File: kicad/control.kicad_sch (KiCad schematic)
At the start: 6 parts, among them U1 ATF22V10C-7PX, U17 SN74F377AN, U2 ATF22V10C-7PX

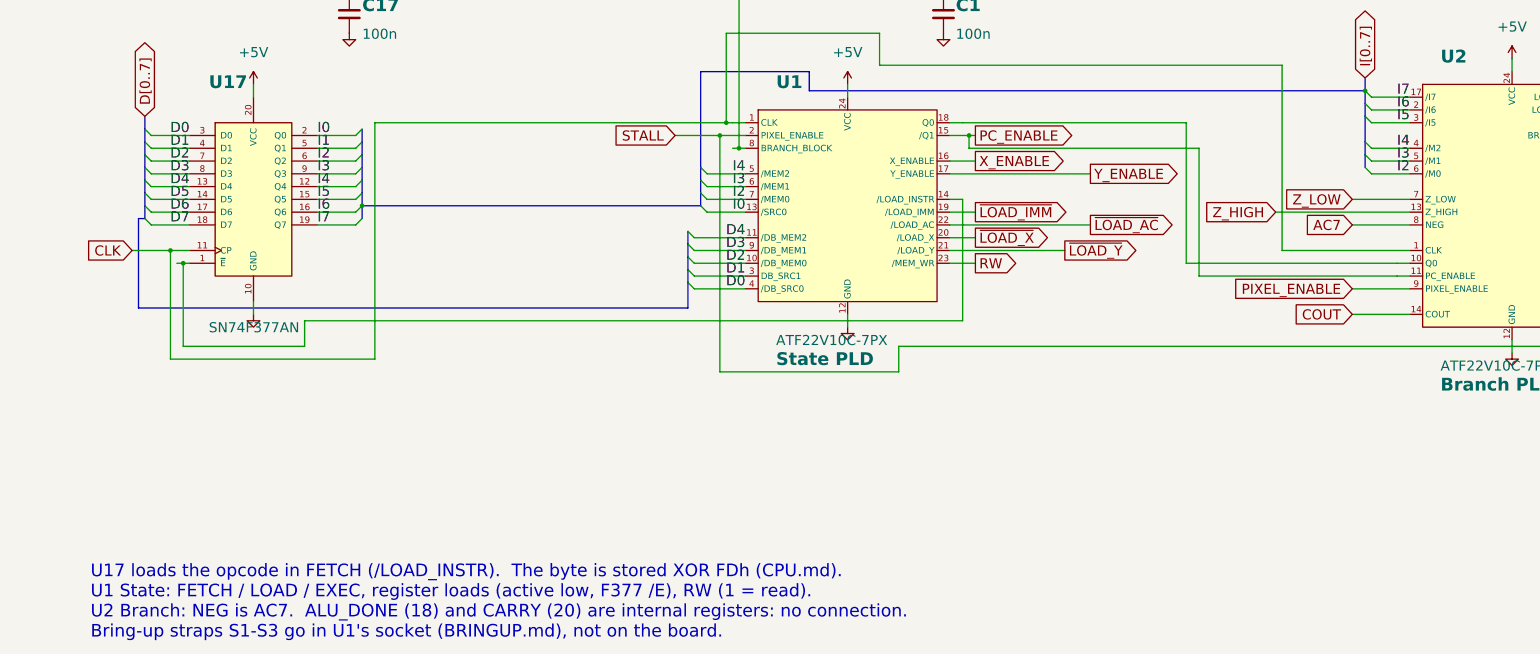
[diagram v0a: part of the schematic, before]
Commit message: Revert the opcode XOR: plain encoding, the cartridge 74AC541 is back
Justin found the inverted opcode bytes too confusing, and a pulled-low
bus is not practical, so this undoes 63a428c:
- opcode bytes are the plain fields again (nop = 02h); the cartridge's
  74AC541 drives 02h while it loads (6 chips, about 33 ms)
- State and Branch PLD revision 15, ALU revision 07 and cartridge PLD
  revision 03 have the same logic as 13, 13, 05 and 01
- read bus pull-ups 10k again; bring-up colour pull-downs 1k
- cartridge schematic gets U6 (74AC541), data bus SIP 10k
- program hex, menu ROM and bring-up ROM reassembled

Kept from 63a428c: RUN starts high in basys_top, the bring-up ROM's
explicit jump to frame_loop, and test_io's con_gets ROM map.

Co-Authored-By: Claude Opus 5.5 (1M context) <noreply@anthropic.com>
Claude-Session: https://claude.ai/code/session_01PNJoPfzmo1tu8EorCrua96
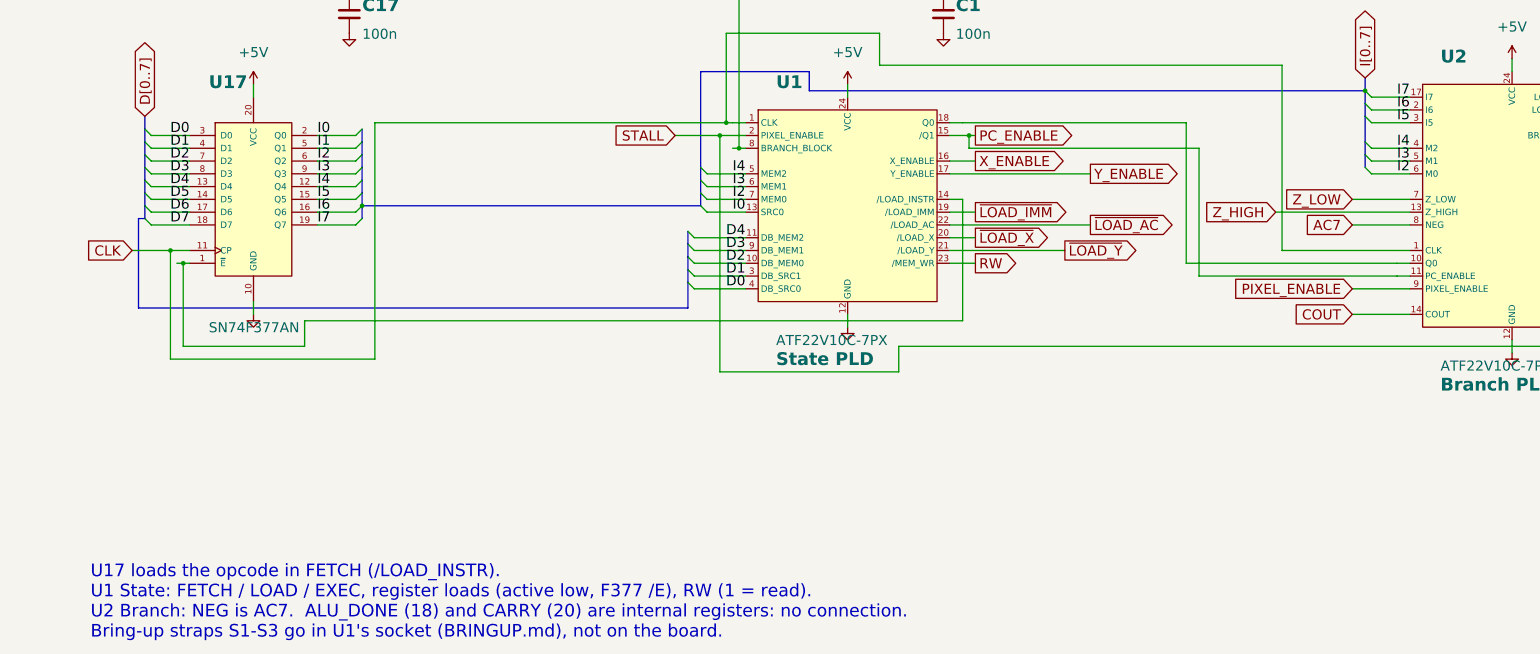
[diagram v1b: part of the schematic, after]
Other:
- note added: "U17 loads the opcode in FETCH (/LOAD_INSTR)."
- note removed: "U17 loads the opcode in FETCH (/LOAD_INSTR). The byte is stored XOR FDh (CPU.md)."
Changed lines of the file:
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@@
 (kicad_sch (version 20230121) (generator eeschema)
   (paper "A3")
-  (title_block (title "Placard: Control") (date "2026-10-20") (rev "1") (company "Placard computer") (comment 1 "Generated by src/scripts/gen_kicad_schematic.py; plan in docs/SCHEMATIC_PLAN.md") (comment 2 "Chip numbers U1-U41 = docs/CHIPS.md; decoupling Cn goes with Un"))
+  (title_block (title "Placard: Control") (date "2026-10-21") (rev "1") (company "Placard computer") (comment 1 "Generated by src/scripts/gen_kicad_schematic.py; plan in docs/SCHEMATIC_PLAN.md") (comment 2 "Chip numbers U1-U41 = docs/CHIPS.md; decoupling Cn goes with Un"))
   (text "Control" (at 15 22 0) (effects (font (size 6 6) bold) (justify left bottom)))
   (text "State and Branch PLDs, instruction register" (at 15 30 0) (effects (font (size 3 3)) (justify left bottom)))
@@
   (symbol (lib_id "power:GND") (at 341.63 96.52 0) (unit 1) (in_bom yes) (on_board yes) (dnp no) (property "Reference" "#PWR0312" (at 341.63 96.52 0) (effects (font (size 1.27 1.27)) hide)) (property "Value" "GND" (at 341.63 102.87 0) (effects (font (size 2 2)) hide)) (property "Footprint" "" (at 341.63 96.52 0) (effects (font (size 1.27 1.27)) hide)) (property "Datasheet" "" (at 341.63 96.52 0) (effects (font (size 1.27 1.27)) hide)) (pin "1") (instances (project "placard" (path "/e3450542-4ffc-59d4-a4a7-45636233928a/370d9988-af17-5e05-8c50-5ef0ca792654" (reference "#PWR0312") (unit 1)))))
   (symbol (lib_id "Device:C") (at 341.63 92.71 0) (unit 1) (in_bom yes) (on_board yes) (dnp no) (property "Reference" "C2" (at 344 92.42 0) (effects (font (size 2.54 2.54) bold) (justify left bottom))) (property "Value" "100n" (at 344 95.52 0) (effects (font (size 2 2)) (justify left top))) (property "Footprint" "Capacitor_THT:C_Disc_D5.0mm_W2.5mm_P5.00mm" (at 341.63 92.71 0) (effects (font (size 1.27 1.27)) hide)) (property "Datasheet" "~" (at 341.63 92.71 0) (effects (font (size 1.27 1.27)) hide)) (pin "1") (pin "2") (instances (project "placard" (path "/e3450542-4ffc-59d4-a4a7-45636233928a/370d9988-af17-5e05-8c50-5ef0ca792654" (reference "C2") (unit 1)))))
-  (text "U17 loads the opcode in FETCH (/LOAD_INSTR).  The byte is stored XOR FDh (CPU.md)." (at 40 205 0) (effects (font (size 2.5 2.5)) (justify left bottom)))
+  (text "U17 loads the opcode in FETCH (/LOAD_INSTR)." (at 40 205 0) (effects (font (size 2.5 2.5)) (justify left bottom)))
   (text "U1 State: FETCH / LOAD / EXEC, register loads (active low, F377 /E), RW (1 = read)." (at 40 209 0) (effects (font (size 2.5 2.5)) (justify left bottom)))
   (text "U2 Branch: NEG is AC7.  ALU_DONE (18) and CARRY (20) are internal registers: no connection." (at 40 213 0) (effects (font (size 2.5 2.5)) (justify left bottom)))

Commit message: Cartridge loader everywhere: FPGA cartridge model, random RAM, nop at x0000
- src/hdl/cartridge.vhd: the ROM cartridge (loader PLD, EEPROMs from
  rom.mem, SRAM written by /SR_WE); basys_top uses it for RUN, STALL_OUT
  and the ROM data, and the IR PLD replaces the instruction F377
- main RAM and cartridge SRAM start random (gen_random_ram.tcl writes
  ram.mem and cart_ram.mem); build, fast and create_project scripts
  updated, new .vhd files are added to an existing project
- rom_boot and the bring-up ROM keep a nop at x0000 for the hand-off;
  menu and bring-up images rebuilt
- schematic: IR PLD as U17, no 74AC32, STALL_IN/STALL_OUT/PC_ENABLE on
  the cartridge connector, cartridge without the 541; PDFs regenerated
- docs: ROM, CHIPS, BRINGUP, EXPANSION, timing, PLD usage, kitting,
  schematic plan, block diagram
- src/sim/tb_top_load.vhd: whole FPGA model from power-up through the
  load and boot

Co-Authored-By: Claude Opus 5.5 (1M context) <noreply@anthropic.com>
Claude-Session: https://claude.ai/code/session_01PNJoPfzmo1tu8EorCrua96
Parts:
- removed U17: SN74F377AN, Package_DIP:DIP-20_W7.62mm, symbol 74xx:74LS377
- added U17: ATF22V10C-7PX, Package_DIP:DIP-24_W7.62mm, symbol placard:ATF22V10C_IR
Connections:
- net +5V: now also U17.24 (VCC)
- net CLK: now also U17.1 (CLK)
- net D0: now also U17.2 (D0)
- net D1: now also U17.3 (D1)
- net D2: now also U17.4 (D2)
- net D3: now also U17.5 (D3)
- net D4: now also U17.6 (D4)
- net D5: now also U17.7 (D5)
- net D6: now also U17.8 (D6)
- net D7: now also U17.9 (D7)
- net GND: now also U17.12 (GND)
- net I0: now also U17.14 (I0)
- net I1: now also U17.15 (I1)
- net I2: now also U17.16 (I2)
- net I3: now also U17.17 (I3)
- net I4: now also U17.18 (I4)
- net I5: now also U17.19 (I5)
- net I6: now also U17.20 (I6)
- net I7: now also U17.21 (I7)
- net at U1.14 (/LOAD_INSTR): now also U17.10 (/LOAD_INSTR)
- net STALL renamed STALL_IN
- net STALL_IN: no longer U1.2 (PIXEL_ENABLE)
- new net RUN: U17.11 (RUN)
- new net STALL_OUT: U1.2 (PIXEL_ENABLE)
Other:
- note added: "U17 loads the opcode in FETCH (/LOAD_INSTR) and holds 02h while RUN is low."
- note added: "U2's STALL (STALL_IN) goes to the cartridge; STALL_OUT comes back to U1 and the PC."
- note removed: "U17 loads the opcode in FETCH (/LOAD_INSTR)."

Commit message: Branch, audio slot and cartridge PLDs to ATF22V10C-10PU
The IR PLD's 5.5 ns clock to output gave the IR-started paths 5 ns, so
the Branch PLD (+4.7 branch decision, +2.2 STALL through the cartridge)
and the audio slot PLD (+5.2 /AC_SEL) fit the -10 grade; the cartridge
loader goes with them (tb_cart_load passes with every PLD at -10).

Co-Authored-By: Claude Opus 5.5 (1M context) <noreply@anthropic.com>
Claude-Session: https://claude.ai/code/session_01PNJoPfzmo1tu8EorCrua96
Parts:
- U2: value ATF22V10C-7PX -> ATF22V10C-10PU
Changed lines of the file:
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@@
 (kicad_sch (version 20230121) (generator eeschema)
   (paper "A3")
-  (title_block (title "Placard: Control") (date "2026-10-21") (rev "1") (company "Placard computer") (comment 1 "Generated by src/scripts/gen_kicad_schematic.py; plan in docs/SCHEMATIC_PLAN.md") (comment 2 "Chip numbers U1-U41 = docs/CHIPS.md; decoupling Cn goes with Un"))
+  (title_block (title "Placard: Control") (date "2026-10-21") (rev "1") (company "Placard computer") (comment 1 "Generated by src/scripts/gen_kicad_schematic.py; plan in docs/SCHEMATIC_PLAN.md") (comment 2 "Chip numbers U1-U40 = docs/CHIPS.md; decoupling Cn goes with Un"))
   (text "Control" (at 15 22 0) (effects (font (size 6 6) bold) (justify left bottom)))
   (text "State and Branch PLDs, instruction register" (at 15 30 0) (effects (font (size 3 3)) (justify left bottom)))
@@
   (wire (pts (xy 322.58 157.48) (xy 322.58 160.02)) (stroke (width 0) (type default)))
   (symbol (lib_id "power:GND") (at 322.58 160.02 0) (unit 1) (in_bom yes) (on_board yes) (dnp no) (property "Reference" "#PWR0310" (at 322.58 160.02 0) (effects (font (size 1.27 1.27)) hide)) (property "Value" "GND" (at 322.58 166.37 0) (effects (font (size 2 2)) hide)) (property "Footprint" "" (at 322.58 160.02 0) (effects (font (size 1.27 1.27)) hide)) (property "Datasheet" "" (at 322.58 160.02 0) (effects (font (size 1.27 1.27)) hide)) (pin "1") (instances (project "placard" (path "/e3450542-4ffc-59d4-a4a7-45636233928a/370d9988-af17-5e05-8c50-5ef0ca792654" (reference "#PWR0310") (unit 1)))))
-  (symbol (lib_id "placard:ATF22V10C_BRANCH") (at 322.58 129.54 0) (unit 1) (in_bom yes) (on_board yes) (dnp no) (property "Reference" "U2" (at 308.356 102.64 0) (effects (font (size 2.54 2.54) bold) (justify left bottom))) (property "Value" "ATF22V10C-7PX" (at 308.356 161.48 0) (effects (font (size 2 2)) (justify left top))) (property "Function" "Branch PLD" (at 308.356 164.88 0) (effects (font (size 2.54 2.54) bold) (justify left top))) (property "Footprint" "Package_DIP:DIP-24_W7.62mm" (at 322.58 129.54 0) (effects (font (size 1.27 1.27)) hide)) (property "Datasheet" "https://ww1.microchip.com/downloads/en/DeviceDoc/doc0735.pdf" (at 322.58 129.54 0) (effects (font (size 1.27 1.27)) hide)) (property "PLD" "ATF22V10_BRANCH.pld" (at 322.58 129.54 0) (effects (font (size 1.27 1.27)) hide)) (pin "17") (pin "2") (pin "3") (pin "4") (pin "5") (pin "6") (pin "7") (pin "13") (pin "8") (pin "1") (pin "10") (pin "11") (pin "9") (pin "14") (pin "21") (pin "22") (pin "23") (pin "19") (pin "16") (pin "15") (pin "18") (pin "20") (pin "24") (pin "12") (instances (project "placard" (path "/e3450542-4ffc-59d4-a4a7-45636233928a/370d9988-af17-5e05-8c50-5ef0ca792654" (reference "U2") (unit 1)))))
+  (symbol (lib_id "placard:ATF22V10C_BRANCH") (at 322.58 129.54 0) (unit 1) (in_bom yes) (on_board yes) (dnp no) (property "Reference" "U2" (at 308.356 102.64 0) (effects (font (size 2.54 2.54) bold) (justify left bottom))) (property "Value" "ATF22V10C-10PU" (at 308.356 161.48 0) (effects (font (size 2 2)) (justify left top))) (property "Function" "Branch PLD" (at 308.356 164.88 0) (effects (font (size 2.54 2.54) bold) (justify left top))) (property "Footprint" "Package_DIP:DIP-24_W7.62mm" (at 322.58 129.54 0) (effects (font (size 1.27 1.27)) hide)) (property "Datasheet" "https://ww1.microchip.com/downloads/en/DeviceDoc/doc0735.pdf" (at 322.58 129.54 0) (effects (font (size 1.27 1.27)) hide)) (property "PLD" "ATF22V10_BRANCH.pld" (at 322.58 129.54 0) (effects (font (size 1.27 1.27)) hide)) (pin "17") (pin "2") (pin "3") (pin "4") (pin "5") (pin "6") (pin "7") (pin "13") (pin "8") (pin "1") (pin "10") (pin "11") (pin "9") (pin "14") (pin "21") (pin "22") (pin "23") (pin "19") (pin "16") (pin "15") (pin "18") (pin "20") (pin "24") (pin "12") (instances (project "placard" (path "/e3450542-4ffc-59d4-a4a7-45636233928a/370d9988-af17-5e05-8c50-5ef0ca792654" (reference "U2") (unit 1)))))
   (symbol (lib_id "power:+5V") (at 341.63 88.9 0) (unit 1) (in_bom yes) (on_board yes) (dnp no) (property "Reference" "#PWR0311" (at 341.63 88.9 0) (effects (font (size 1.27 1.27)) hide)) (property "Value" "+5V" (at 341.63 82.55 0) (effects (font (size 2 2)))) (property "Footprint" "" (at 341.63 88.9 0) (effects (font (size 1.27 1.27)) hide)) (property "Datasheet" "" (at 341.63 88.9 0) (effects (font (size 1.27 1.27)) hide)) (pin "1") (instances (project "placard" (path "/e3450542-4ffc-59d4-a4a7-45636233928a/370d9988-af17-5e05-8c50-5ef0ca792654" (reference "#PWR0311") (unit 1)))))
   (symbol (lib_id "power:GND") (at 341.63 96.52 0) (unit 1) (in_bom yes) (on_board yes) (dnp no) (property "Reference" "#PWR0312" (at 341.63 96.52 0) (effects (font (size 1.27 1.27)) hide)) (property "Value" "GND" (at 341.63 102.87 0) (effects (font (size 2 2)) hide)) (property "Footprint" "" (at 341.63 96.52 0) (effects (font (size 1.27 1.27)) hide)) (property "Datasheet" "" (at 341.63 96.52 0) (effects (font (size 1.27 1.27)) hide)) (pin "1") (instances (project "placard" (path "/e3450542-4ffc-59d4-a4a7-45636233928a/370d9988-af17-5e05-8c50-5ef0ca792654" (reference "#PWR0312") (unit 1)))))
